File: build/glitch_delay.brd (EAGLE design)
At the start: 101.3 x 64.8 mm, 55 parts

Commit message: Removing PIC from board and using ADC1.
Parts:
- removed C2: 0.1uF, adafruit:C025-030X050
- removed JP1: (no value), adafruit:1X06
- removed LED4: (no value), adafruit:LED3MM
- removed PIC: PIC16F1825DIL14, jasons_stuff:DIL14
- removed R10, R11: 4.7k, MusicThingModular:7MM_RESISTOR
- removed R16: 1k, MusicThingModular:7MM_RESISTOR
- moved VR1 2.86 mm to (64.8, 25.1), turned to 180 degrees
- moved VR2 2.86 mm to (50.5, 25.1), turned to 180 degrees
- moved VR3 2.86 mm to (36.3, 25.1), turned to 180 degrees
- moved VR4 2.86 mm to (22.3, 25.1), turned to 180 degrees
- moved VR5 2.86 mm to (8.35, 25.1), turned to 180 degrees
- moved VR6 2.86 mm to (79.0, 25.1), turned to 180 degrees
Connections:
- removed net MCLR: JP1.1, PIC.4
- removed net N$1: LED4.A, R16.1
- removed net N$10: PIC.11, VR3.2
- removed net N$11: PIC.8, VR4.2
- removed net N$12: PIC.3, VR5.2
- removed net N$15: PIC.7, VR6.2
- removed net N$5: PIC.2, R16.2
- removed net PGC: JP1.5, PIC.12, VR2.2
- removed net PGD: JP1.4, PIC.13, VR1.2
- new net POT1: U$1.35/A16, VR1.2
- new net POT2: U$1.36/A17, VR2.2
- new net POT3: U$1.37/A18, VR3.2
- new net POT4: U$1.38/A19, VR4.2
- new net POT5: U$1.39/A20, VR5.2
- new net POT6: U$1.32/A13, VR6.2
- net 3.3V: no longer C2.2, JP1.2, PIC.1, R10.2, R11.2
- net GND: no longer C2.1, JP1.3, LED4.K, PIC.14
- net SCL: no longer PIC.10, R10.1, U$1.19/A5/SCL
- net SDA: no longer PIC.9, R11.1, U$1.18/A4/SDA
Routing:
- net SDA: track 218.9 -> 0.00 mm, vias 2 -> 0
- net SCL: track 203.2 -> 0.00 mm
- net N$12: track 89.6 -> 0.00 mm
- net N$11: track 82.9 -> 0.00 mm
- net PGC: track 65.0 -> 0.00 mm
- net N$10: track 64.9 -> 0.00 mm
- net 3.3V: track 203.0 -> 147.6 mm
- net PGD: track 49.5 -> 0.00 mm
- net POT5: track 0.00 -> 41.8 mm
- net POT6: track 0.00 -> 34.3 mm, vias 0 -> 1
- net POT4: track 0.00 -> 32.6 mm
- net N$5: track 31.8 -> 0.00 mm
- net POT3: track 0.00 -> 19.2 mm
- net N$15: track 13.6 -> 0.00 mm
- net MCLR: track 11.8 -> 0.00 mm
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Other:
- board size 101.3 x 64.8 mm -> 101.3 x 58.1 mm
- board text added: "Cutlassiezer 2.1 Scott Pitkethly Tom Armitage"
- board text removed: "Cutlassiezer v2 - Scott Pitkethly"

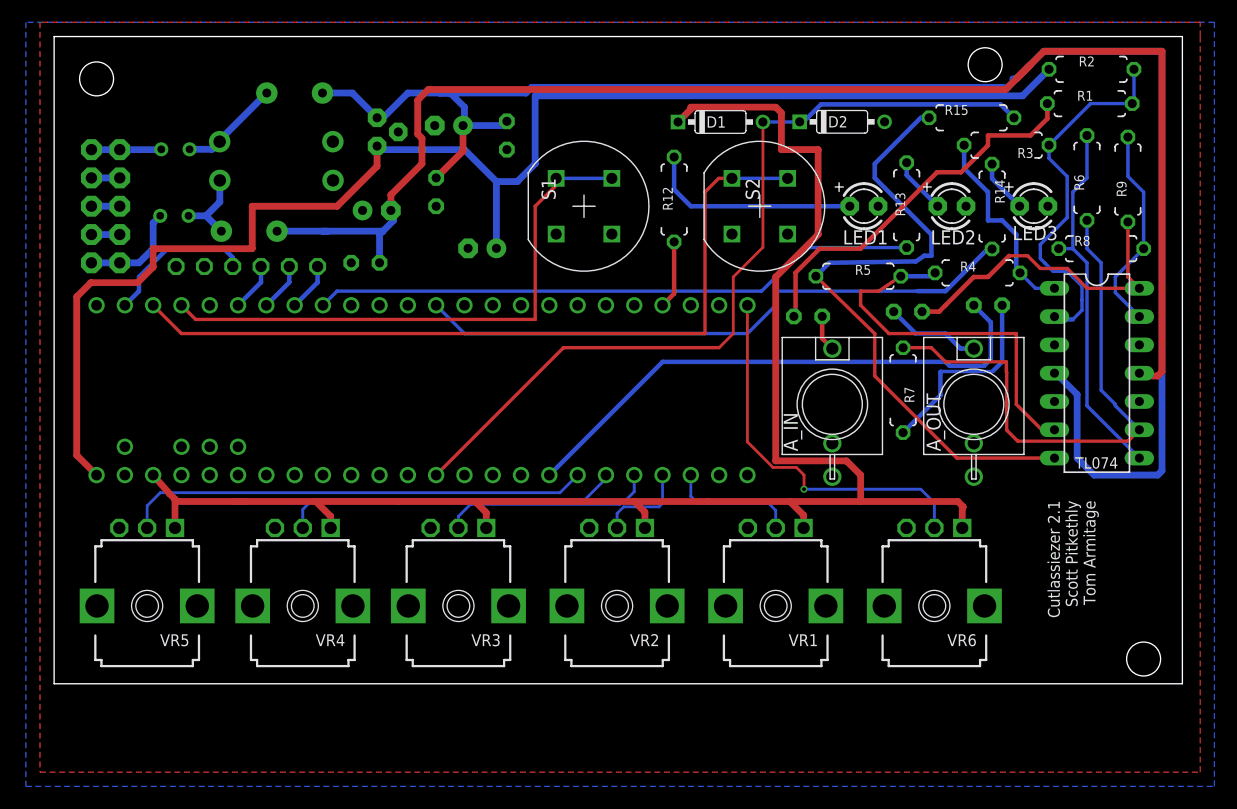
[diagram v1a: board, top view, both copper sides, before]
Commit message: Minor schematic tidying.
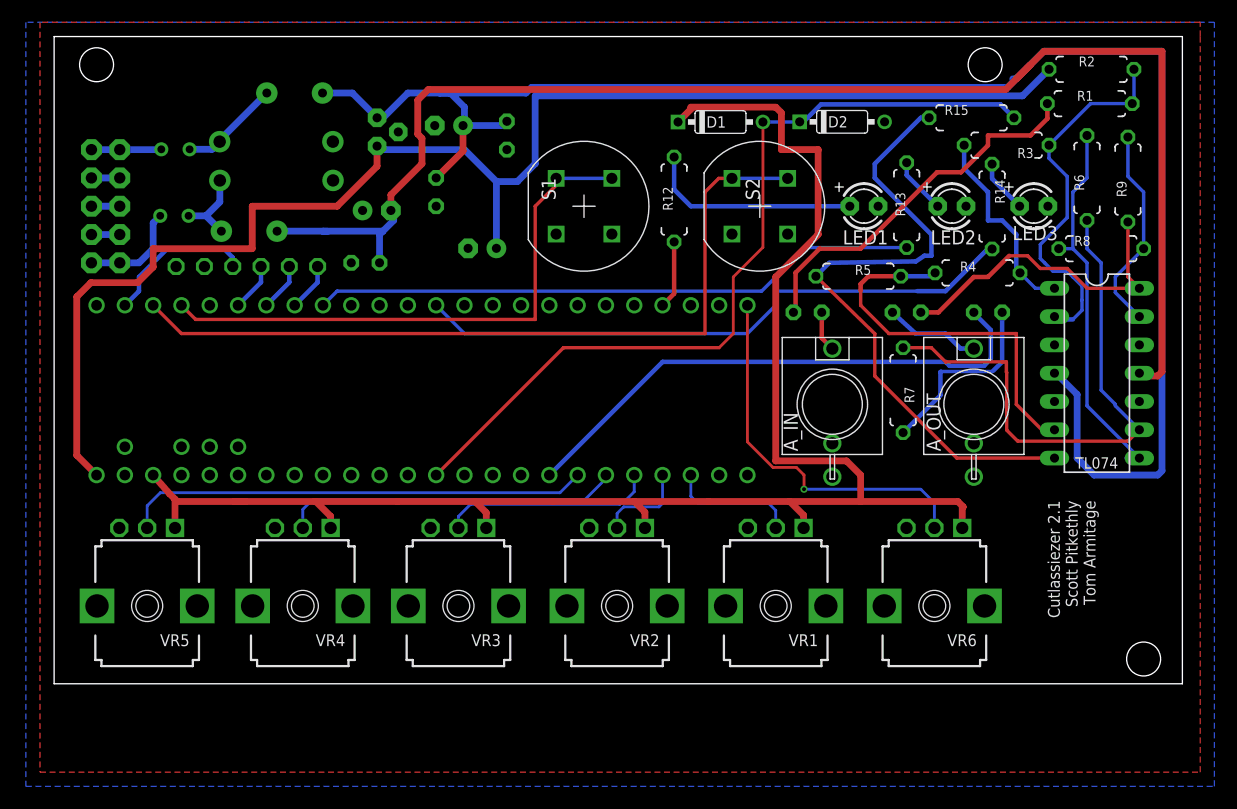
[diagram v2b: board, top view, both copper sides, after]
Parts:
- moved C3 0.63 mm to (83.8, 51.4)
- moved C1 0.37 mm to (67.6, 51.4)
- moved C4 0.13 mm to (76.5, 51.4)
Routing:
- net N$13: track 17.8 -> 17.2 mm
- net DAC0: track 49.7 -> 49.1 mm
- net N$6: track 34.2 -> 34.8 mm
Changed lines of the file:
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@@
 Scott Pitkethly
 Tom Armitage</text>
-<hole x="3.81" y="72.39" drill="3.048"/>
+<hole x="3.81" y="73.66" drill="3.048"/>
 <hole x="83.566" y="73.66" drill="3.048"/>
 <hole x="97.79" y="20.32" drill="3.048"/>
@@
 </autorouter>
 <elements>
-<element name="C1" library="adafruit" package="C025-030X050" value="0.1uF" x="67.67" y="51.07" smashed="yes" rot="MR180">
-<attribute name="NAME" x="65.384" y="49.165" size="1.27" layer="26" ratio="10" rot="MR180"/>
-<attribute name="VALUE" x="65.384" y="54.118" size="1.27" layer="28" ratio="10" rot="MR180"/>
+<element name="C1" library="adafruit" package="C025-030X050" value="0.1uF" x="67.6275" y="51.435" smashed="yes" rot="MR180">
+<attribute name="NAME" x="65.3415" y="49.53" size="1.27" layer="26" ratio="10" rot="MR180"/>
+<attribute name="VALUE" x="65.3415" y="54.483" size="1.27" layer="28" ratio="10" rot="MR180"/>
 </element>
 <element name="C10" library="adafruit" package="C025-030X050" value="0.1uF" x="27.94" y="55.88" smashed="yes" rot="MR180">
@@
 <attribute name="VALUE" x="25.654" y="58.928" size="1.27" layer="28" ratio="10" rot="MR180"/>
 </element>
-<element name="C3" library="adafruit" package="C025-030X050" value="0.1uF" x="83.82" y="52.07" smashed="yes" rot="MR0">
-<attribute name="NAME" x="86.106" y="48.895" size="1.27" layer="26" ratio="10" rot="MR0"/>
-<attribute name="VALUE" x="86.106" y="49.022" size="1.27" layer="28" ratio="10" rot="MR0"/>
-</element>
-<element name="C4" library="adafruit" package="C025-030X050" value="10uF" x="76.63" y="51.5" smashed="yes" rot="MR180">
-<attribute name="NAME" x="78.154" y="49.595" size="1.27" layer="26" ratio="10" rot="MR180"/>
-<attribute name="VALUE" x="74.344" y="54.548" size="1.27" layer="28" ratio="10" rot="MR180"/>
+<element name="C3" library="adafruit" package="C025-030X050" value="0.1uF" x="83.82" y="51.435" smashed="yes" rot="MR0">
+<attribute name="NAME" x="86.106" y="48.26" size="1.27" layer="26" ratio="10" rot="MR0"/>
+<attribute name="VALUE" x="86.106" y="48.387" size="1.27" layer="28" ratio="10" rot="MR0"/>
+</element>
+<element name="C4" library="adafruit" package="C025-030X050" value="10uF" x="76.5175" y="51.435" smashed="yes" rot="MR180">
+<attribute name="NAME" x="78.0415" y="49.53" size="1.27" layer="26" ratio="10" rot="MR180"/>
+<attribute name="VALUE" x="74.2315" y="54.483" size="1.27" layer="28" ratio="10" rot="MR180"/>
 </element>
 <element name="C5" library="adafruit" package="E2,5-6E" value="10uF" x="35.433" y="68.199" smashed="yes" rot="MR0">
@@
 <contactref element="A_IN" pad="P$1_TIP"/>
 <contactref element="C1" pad="2"/>
-<wire x1="69.85" y1="48.18" x2="68.94" y2="49.09" width="0.4064" layer="1"/>
-<wire x1="68.94" y1="49.09" x2="68.94" y2="51.07" width="0.4064" layer="1"/>
+<wire x1="68.903253125" y1="51.117603125" x2="68.8975" y2="51.435" width="0.4064" layer="1"/>
+<wire x1="68.903253125" y1="49.126746875" x2="68.903253125" y2="51.117603125" width="0.4064" layer="1"/>
+<wire x1="69.85" y1="48.18" x2="68.903253125" y2="49.126746875" width="0.4064" layer="1"/>
 </signal>
 <signal name="N$4">
@@
 <wire x1="88.646" y1="40.894" x2="86.36" y2="43.18" width="0.3048" layer="1"/>
 <wire x1="86.36" y1="43.18" x2="86.36" y2="49.53" width="0.3048" layer="1"/>
-<wire x1="86.36" y1="49.53" x2="74.93" y2="49.53" width="0.3048" layer="1"/>
+<wire x1="86.36" y1="49.53" x2="84.1375" y2="49.53" width="0.3048" layer="1"/>
+<wire x1="84.1375" y1="49.53" x2="83.82" y2="49.53" width="0.3048" layer="1"/>
+<wire x1="83.82" y1="49.53" x2="74.93" y2="49.53" width="0.3048" layer="1"/>
 <wire x1="74.93" y1="49.53" x2="72.39" y2="52.07" width="0.3048" layer="1"/>
-<wire x1="72.39" y1="52.07" x2="72.39" y2="53.34" width="0.3048" layer="1"/>
-<wire x1="72.39" y1="53.34" x2="74.022" y2="53.34" width="0.3048" layer="1"/>
-<wire x1="74.022" y1="53.34" x2="75.994" y2="54.677" width="0.3048" layer="1"/>
+<wire x1="72.39" y1="53.34" x2="72.39" y2="52.07" width="0.3048" layer="1"/>
 <wire x1="75.994" y1="54.677" x2="78.773" y2="54.677" width="0.4064" layer="16"/>
 <wire x1="78.773" y1="54.677" x2="79.075" y2="54.979" width="0.4064" layer="16"/>
+<wire x1="75.994" y1="54.677" x2="73.092" y2="54.677" width="0.4064" layer="1"/>
+<wire x1="73.092" y1="54.677" x2="72.39" y2="53.975" width="0.4064" layer="1"/>
+<wire x1="72.39" y1="53.975" x2="72.39" y2="53.34" width="0.4064" layer="1"/>
 </signal>
 <signal name="N$3">
@@
 <wire x1="68.707" y1="57.15" x2="66.548" y2="54.991" width="0.4064" layer="1"/>
 <wire x1="66.548" y1="54.991" x2="66.548" y2="51.218" width="0.4064" layer="1"/>
-<wire x1="66.548" y1="51.218" x2="66.4" y2="51.07" width="0.4064" layer="1"/>
+<wire x1="66.548" y1="51.218" x2="66.3575" y2="51.435" width="0.4064" layer="1"/>
 </signal>
 <signal name="N$8">
@@
 <contactref element="C3" pad="2"/>
 <contactref element="U$1" pad="21/DAC0"/>
-<wire x1="84.074" y1="47.244" x2="84.074" y2="50.546" width="0.4064" layer="16"/>
+<wire x1="84.074" y1="47.244" x2="84.074" y2="49.8475" width="0.4064" layer="16"/>
 <wire x1="83.46169375" y1="46.63169375" x2="80.36830625" y2="46.63169375" width="0.4064" layer="16"/>
 <wire x1="80.36830625" y1="46.63169375" x2="80.01" y2="46.99" width="0.4064" layer="16"/>
@@
 <wire x1="54.61" y1="46.99" x2="44.45" y2="36.83" width="0.4064" layer="16"/>
 <wire x1="84.074" y1="47.244" x2="83.46169375" y2="46.63169375" width="0.4064" layer="16"/>
-<wire x1="84.074" y1="50.546" x2="82.55" y2="52.07" width="0.4064" layer="16"/>
+<wire x1="84.074" y1="49.8475" x2="82.55" y2="51.3715" width="0.4064" layer="16"/>
+<wire x1="82.55" y1="51.3715" x2="82.55" y2="51.435" width="0.4064" layer="16"/>
 </signal>
 <signal name="N$13">
@@
 <wire x1="79.606315625" y1="46.123684375" x2="84.223684375" y2="46.123684375" width="0.3048" layer="16"/>
 <wire x1="84.223684375" y1="46.123684375" x2="84.2832" y2="46.1832" width="0.3048" layer="16"/>
-<wire x1="85.09" y1="46.99" x2="85.09" y2="52.07" width="0.4064" layer="16"/>
+<wire x1="85.09" y1="46.99" x2="85.09" y2="51.435" width="0.4064" layer="16"/>
 </signal>
 <signal name="N$14">
@@
 <wire x1="88.519" y1="55.372" x2="87.376" y2="56.515" width="0.3048" layer="1"/>
 <wire x1="85.725" y1="56.515" x2="87.376" y2="56.515" width="0.3048" layer="1"/>
-<wire x1="79.44" y1="51.5" x2="80.01" y2="52.07" width="0.4064" layer="1"/>
-<wire x1="80.01" y1="52.07" x2="82.55" y2="54.61" width="0.4064" layer="1"/>
 <wire x1="82.55" y1="54.61" x2="83.82" y2="54.61" width="0.4064" layer="1"/>
 <wire x1="83.82" y1="54.61" x2="85.725" y2="56.515" width="0.4064" layer="1"/>
-<wire x1="77.9" y1="51.5" x2="79.44" y2="51.5" width="0.4064" layer="1"/>
+<wire x1="77.7875" y1="51.435" x2="79.375" y2="51.435" width="0.4064" layer="1"/>
+<wire x1="79.375" y1="51.435" x2="82.55" y2="54.61" width="0.4064" layer="1"/>
 </signal>
 <signal name="N$22">
@@
 <wire x1="81.36" y1="48.18" x2="80.01" y2="49.53" width="0.4064" layer="16"/>
 <wire x1="80.01" y1="49.53" x2="77.33" y2="49.53" width="0.4064" layer="16"/>
-<wire x1="77.33" y1="49.53" x2="75.36" y2="51.5" width="0.4064" layer="16"/>
+<wire x1="77.33" y1="49.53" x2="75.2475" y2="51.435" width="0.4064" layer="16"/>
 </signal>
 <signal name="SCL">

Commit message: Lots of board tidying.
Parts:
- moved R14 29.0 mm to (55.2, 60.3)
- moved S1 27.0 mm to (27.2, 43.2)
- moved S2 25.8 mm to (44.6, 43.2)
- moved R13 24.5 mm to (52.1, 60.3)
- moved R2 12.6 mm to (84.5, 64.1), turned to 270 degrees
- moved LED1 11.1 mm to (61.6, 61.0)
- moved LED2 11.0 mm to (69.5, 61.0)
- moved LED3 10.5 mm to (77.5, 61.0)
- moved R1 8.27 mm to (87.3, 64.1), turned to 90 degrees
- moved R12 6.87 mm to (48.9, 60.3)
- moved R3 5.22 mm to (90.2, 64.1), turned to 270 degrees
- moved R15 4.82 mm to (81.6, 64.1), turned to 90 degrees
- moved SV1 1.27 mm to (4.62, 62.2)
- moved R9 0.92 mm to (95.9, 64.1)
- moved R6 0.71 mm to (93.0, 64.1)
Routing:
- net N$27: track 54.8 -> 22.8 mm
- net N$20: track 50.7 -> 21.3 mm
- net N$25: track 71.2 -> 42.4 mm
- net N$26: track 54.5 -> 30.3 mm
- net N$23: track 4.81 -> 22.3 mm
- net N$19: track 5.06 -> 19.7 mm
- net N$8: track 58.3 -> 45.9 mm
- net N$4: track 17.9 -> 10.5 mm
- net 5V: track 128.9 -> 122.7 mm
- net -12V: track 128.0 -> 122.9 mm
- net 3.3V: track 147.6 -> 143.0 mm
- net N$9: track 19.3 -> 15.3 mm
- net +12V: track 148.1 -> 145.0 mm
- net A0: track 76.1 -> 73.5 mm
- net N$17: track 6.12 -> 7.56 mm
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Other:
- board size 101.3 x 58.1 mm -> 101 x 55.2 mm

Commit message: Much smaller.
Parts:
- moved C10 72.4 mm to (97.2, 34.6), turned to 0 degrees
- moved C9 59.9 mm to (90.8, 34.6), turned to 0 degrees
- moved FU2 8.38 mm to (7.30, 67.7)
- moved C5 7.31 mm to (42.7, 67.9)
- moved C8 5.91 mm to (33.7, 57.1)
- moved SV1 4.61 mm to (9.21, 61.8), turned to 0 degrees
- moved C6 4.46 mm to (42.9, 57.5)
- moved VREG 4.13 mm to (32.8, 66.0)
- moved FER2 3.81 mm to (21.3, 58.7)
- moved FER1 3.62 mm to (24.4, 68.9)
- moved D3 3.62 mm to (23.4, 65.8)
- moved D4 3.55 mm to (23.4, 62.6)
- moved FU1 2.73 mm to (13.1, 67.7)
- moved C7 2.56 mm to (36.8, 62.5)
- moved D1 2.54 mm to (59.8, 66.0)
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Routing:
- net N$30: track 7.21 -> 16.1 mm
- net +12V: track 145.0 -> 138.2 mm
- net +12V_IN: track 6.78 -> 13.1 mm
- net -12V: track 122.9 -> 128.5 mm
- net -12V_IN: track 8.20 -> 12.8 mm
- net A0: track 73.5 -> 69.5 mm
- net 3.3V: track 143.0 -> 145.4 mm
- net N$29: track 9.10 -> 11.3 mm
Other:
- board size 101 x 55.2 mm -> 101 x 53 mm
